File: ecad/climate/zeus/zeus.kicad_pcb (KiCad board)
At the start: 2 copper layers, 80 x 45 mm, 73 parts, among them J1 MCV 1,5/ 2-G-3,5, J10 47053-1000, J11 47053-1000, J2 MCV 1,5/ 2-G-3,5, J3 MCV 1,5/ 2-G-3,5, J4 M20-8760342, J5 47053-1000, J6 47053-1000, J7 215079-8, J8 640454-2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

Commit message: Makes pleiades zeus again
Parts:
- added R20: 47k5, Resistor_SMD:R_0603_1608Metric, F.Cu at (162.3, 139.3)
- added R21: 47k5, Resistor_SMD:R_0603_1608Metric, F.Cu at (169.6, 139.3)
- moved Q1 0.76 mm to (159.8, 139.3)
- moved Q2 0.58 mm to (167.0, 139.3)
- moved D1 0.36 mm to (156.8, 139.3)
- moved D2 0.32 mm to (164.1, 139.3)
- renumbered D2 to D1, D1 to D2
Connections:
- net /HEAT1_PWR renamed /12V Low Side 1/12V_SW-
- net /HEAT2_PWR renamed /12V Low Side 2/12V_SW-
- net /UC/HEAT1 renamed /12V Low Side 1/CMD
- net /UC/HEAT2 renamed /12V Low Side 2/CMD
- U2 pad 1: Net-(U2-Pad1) -> (no net)
- U2 pad 10: Net-(U2-Pad10) -> (no net)
- U2 pad 12: Net-(U2-Pad12) -> (no net)
- U2 pad 13: Net-(U2-Pad13) -> (no net)
- U2 pad 14: Net-(U2-Pad14) -> (no net)
- U2 pad 17: Net-(U2-Pad17) -> (no net)
- U2 pad 18: Net-(U2-Pad18) -> (no net)
- U2 pad 19: Net-(U2-Pad19) -> (no net)
- U2 pad 27: Net-(U2-Pad27) -> (no net)
- U2 pad 28: Net-(U2-Pad28) -> (no net)
- U2 pad 29: Net-(U2-Pad29) -> (no net)
- U2 pad 32: Net-(U2-Pad32) -> (no net)
- U2 pad 33: Net-(U2-Pad33) -> (no net)
- U2 pad 34: Net-(U2-Pad34) -> (no net)
- U2 pad 35: Net-(U2-Pad35) -> (no net)
- U2 pad 36: Net-(U2-Pad36) -> (no net)
- U2 pad 37: Net-(U2-Pad37) -> (no net)
- U2 pad 38: Net-(U2-Pad38) -> (no net)
- U2 pad 39: Net-(U2-Pad39) -> (no net)
- U2 pad 4: Net-(U2-Pad4) -> (no net)
- U2 pad 40: Net-(U2-Pad40) -> (no net)
- U2 pad 41: Net-(U2-Pad41) -> (no net)
- U2 pad 42: Net-(U2-Pad42) -> (no net)
- U2 pad 43: Net-(U2-Pad43) -> (no net)
- U2 pad 44: Net-(U2-Pad44) -> (no net)
- U2 pad 45: Net-(U2-Pad45) -> (no net)
- U2 pad 46: Net-(U2-Pad46) -> (no net)
- U2 pad 47: Net-(U2-Pad47) -> (no net)
- U2 pad 48: Net-(U2-Pad48) -> (no net)
- U2 pad 49: Net-(U2-Pad49) -> (no net)
- U2 pad 50: Net-(U2-Pad50) -> (no net)
- U2 pad 51: Net-(U2-Pad51) -> (no net)
- U2 pad 54: Net-(U2-Pad54) -> (no net)
- U2 pad 55: Net-(U2-Pad55) -> (no net)
- U2 pad 56: Net-(U2-Pad56) -> (no net)
- U2 pad 57: Net-(U2-Pad57) -> (no net)
- U2 pad 58: Net-(U2-Pad58) -> (no net)
- U2 pad 59: Net-(U2-Pad59) -> (no net)
- U2 pad 60: Net-(U2-Pad60) -> (no net)
- U2 pad 61: Net-(U2-Pad61) -> (no net)
- U2 pad 62: Net-(U2-Pad62) -> (no net)
- U2 pad 7: Net-(U2-Pad7) -> (no net)
- U2 pad 9: Net-(U2-Pad9) -> (no net)
- U3 pad 5: Net-(U3-Pad5) -> (no net)
- U5 pad 15: Net-(U5-Pad15) -> (no net)
- U5 pad 16: Net-(U5-Pad16) -> (no net)
- U6 pad 4: /Fan PWM Controller 1/PWM1 -> GND
- U6 pad 5: (no net) -> /Fan PWM Controller 1/PWM1
- U61 pad 4: /Fan PWM Controller 2/PWM1 -> GND
- U61 pad 5: (no net) -> /Fan PWM Controller 2/PWM1
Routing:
- net GND: track 466.1 -> 501.3 mm
- net /12V Low Side 2/CMD: track 27.9 -> 29.3 mm
- net /12V Low Side 1/CMD: track 23.6 -> 24.7 mm
- net /12V Low Side 2/12V_SW-: track 9.40 -> 8.52 mm
- net /12V Low Side 1/12V_SW-: track 9.40 -> 8.70 mm
- net /Fan PWM Controller 2/PWM1: track 15.4 -> 15.9 mm
- net +12V: track 124.4 -> 123.9 mm
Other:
- board text added: "FORT Zeus rev A"
- board text removed: "FORT Pleiades rev A"

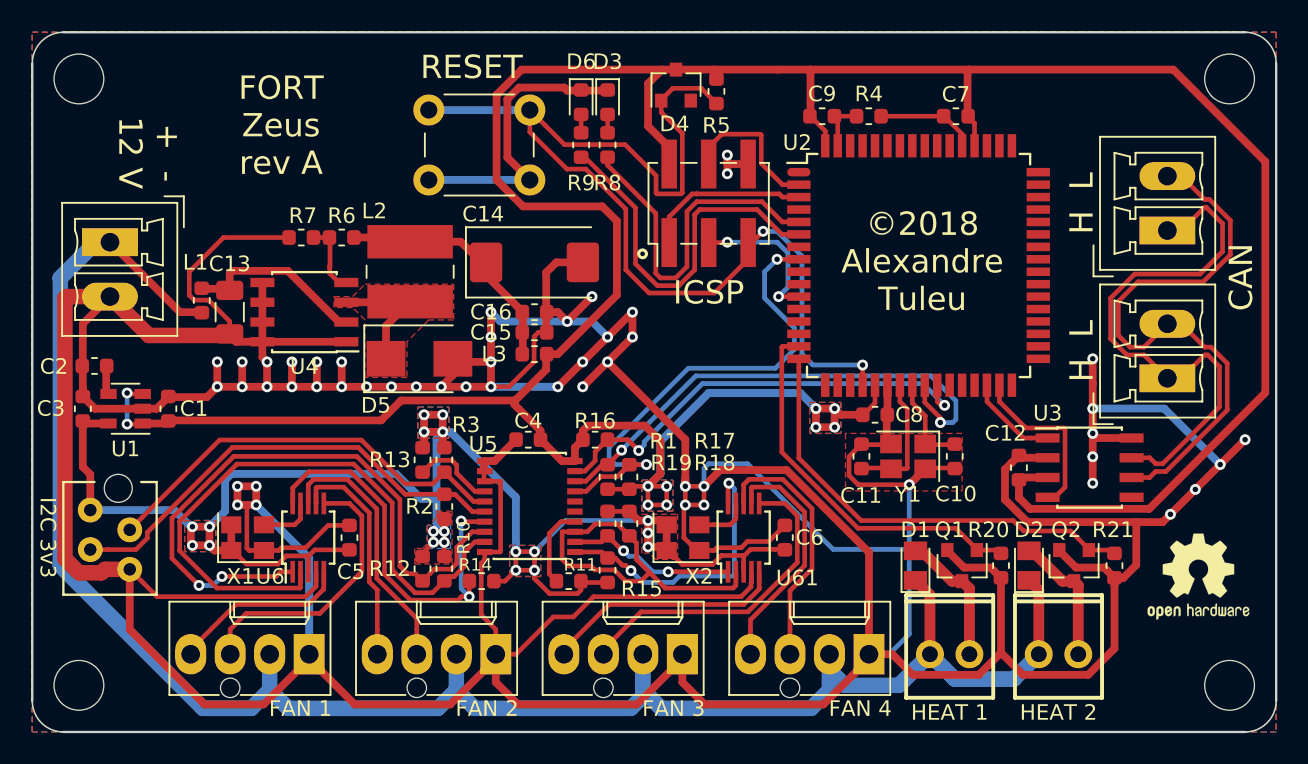
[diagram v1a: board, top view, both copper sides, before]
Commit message: Updates Via size to conform to Factory Capabilities
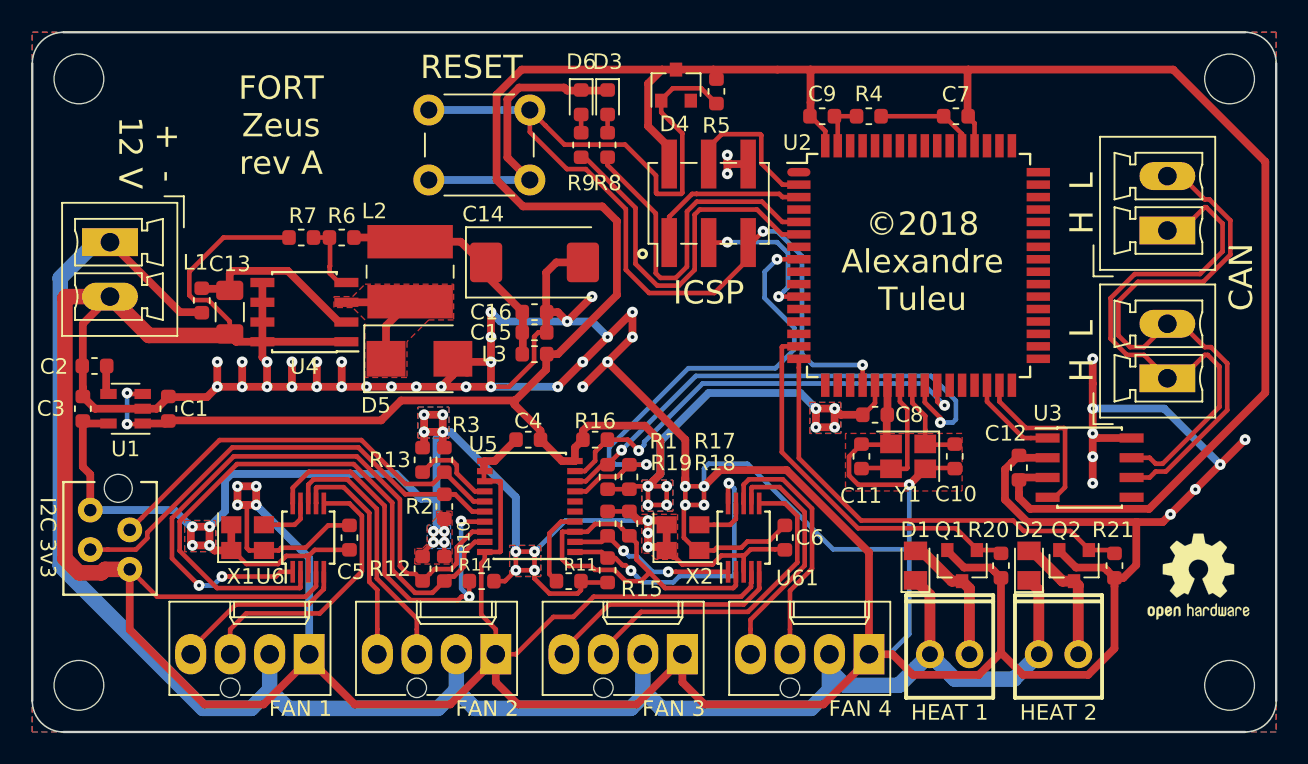
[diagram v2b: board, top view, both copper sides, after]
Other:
- net class Default: via_drill 0.35 -> 0.25
- net class Power: via_drill 0.35 -> 0.25
- rule via_min_drill: 0.35 -> 0.25

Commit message: Small Correction for Production
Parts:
- D1, D2: value MCL4148 -> 1N4148WS; footprint Diode_SMD:D_MicroMELF -> Diode_SMD:D_SOD-323F
- R7: value 4k7 -> 4k87
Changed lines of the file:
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@@
     (visible_elements FFFFFF7F)
     (pcbplotparams
-      (layerselection 0x00030_80000001)
-      (usegerberextensions false)
+      (layerselection 0x010fc_ffffffff)
+      (usegerberextensions true)
       (usegerberattributes false)
       (usegerberadvancedattributes false)
@@
       (psa4output false)
       (plotreference true)
-      (plotvalue true)
+      (plotvalue false)
       (plotinvisibletext false)
       (padsonsilk false)
@@
       (outputformat 1)
       (mirror false)
-      (drillshape 1)
+      (drillshape 0)
       (scaleselection 1)
-      (outputdirectory ""))
+      (outputdirectory "output/"))
   )
   (net 0 "")
@@
     )
   )
-  (module Diode_SMD:D_MicroMELF (layer F.Cu)
-    (at 164.1 139.3 90)
-    (descr "Diode, MicroMELF, http://www.vishay.com/docs/85597/bzm55-se.pdf")
-    (tags "MicroMELF Diode")
-    (attr smd)
-    (fp_text reference D2 (at 2.3 0 180) (layer F.SilkS)
-      (effects (font (size 1 1) (thickness 0.15)))
-    )
-    (fp_text value MCL4148 (at 0 1.8 90) (layer F.Fab)
-      (effects (font (size 1 1) (thickness 0.15)))
-    )
-    (fp_line (start 1.8 1) (end -1.8 1) (layer F.CrtYd) (width 0.05))
-    (fp_line (start 1.8 1) (end 1.8 -1) (layer F.CrtYd) (width 0.05))
-    (fp_line (start -1.8 -1) (end -1.8 1) (layer F.CrtYd) (width 0.05))
-    (fp_line (start -1.8 -1) (end 1.8 -1) (layer F.CrtYd) (width 0.05))
-    (fp_line (start -1.1 0.55) (end -1.1 -0.55) (layer F.Fab) (width 0.12))
-    (fp_line (start 1.1 0.55) (end -1.1 0.55) (layer F.Fab) (width 0.12))
-    (fp_line (start 1.1 -0.55) (end 1.1 0.55) (layer F.Fab) (width 0.12))
-    (fp_line (start -1.1 -0.55) (end 1.1 -0.55) (layer F.Fab) (width 0.12))
-    (fp_line (start -0.6 -0.55) (end -0.6 0.55) (layer F.Fab) (width 0.12))
-    (fp_text user %R (at 0 -1.7 90) (layer F.Fab)
-      (effects (font (size 1 1) (thickness 0.15)))
-    )
-    (fp_line (start -0.25 -0.25) (end -0.25 0.25) (layer F.Fab) (width 0.12))
-    (fp_line (start -0.25 0) (end -0.75 0) (layer F.Fab) (width 0.12))
-    (fp_line (start 0.25 0.25) (end -0.25 0) (layer F.Fab) (width 0.12))
-    (fp_line (start 0.25 -0.25) (end 0.25 0.25) (layer F.Fab) (width 0.12))
-    (fp_line (start -0.25 0) (end 0.25 -0.25) (layer F.Fab) (width 0.12))
-    (fp_line (start 0.25 0) (end 0.75 0) (layer F.Fab) (width 0.12))
-    (fp_line (start -1.7 0.9) (end 1.1 0.9) (layer F.SilkS) (width 0.12))
-    (fp_line (start -1.7 -0.9) (end -1.7 0.9) (layer F.SilkS) (width 0.12))
-    (fp_line (start 1.1 -0.9) (end -1.7 -0.9) (layer F.SilkS) (width 0.12))
-    (pad 2 smd rect (at 0.95 0 90) (size 1.2 1.5) (layers F.Cu F.Paste F.Mask)
-      (net 49 "/12V Low Side 2/12V_SW-"))
-    (pad 1 smd rect (at -0.95 0 90) (size 1.2 1.5) (layers F.Cu F.Paste F.Mask)
-      (net 8 +12V))
-    (model ${KISYS3DMOD}/Diode_SMD.3dshapes/D_MicroMELF.wrl
-      (at (xyz 0 0 0))
-      (scale (xyz 1 1 1))
-      (rotate (xyz 0 0 0))
-    )
-  )
-  (module Diode_SMD:D_MicroMELF (layer F.Cu)
-    (at 156.8 139.3 90)
-    (descr "Diode, MicroMELF, http://www.vishay.com/docs/85597/bzm55-se.pdf")
-    (tags "MicroMELF Diode")
-    (attr smd)
-    (fp_text reference D1 (at 2.3 0 180) (layer F.SilkS)
-      (effects (font (size 1 1) (thickness 0.15)))
-    )
-    (fp_text value MCL4148 (at 0 1.8 90) (layer F.Fab)
-      (effects (font (size 1 1) (thickness 0.15)))
-    )
-    (fp_line (start 1.8 1) (end -1.8 1) (layer F.CrtYd) (width 0.05))
-    (fp_line (start 1.8 1) (end 1.8 -1) (layer F.CrtYd) (width 0.05))
-    (fp_line (start -1.8 -1) (end -1.8 1) (layer F.CrtYd) (width 0.05))
-    (fp_line (start -1.8 -1) (end 1.8 -1) (layer F.CrtYd) (width 0.05))
-    (fp_line (start -1.1 0.55) (end -1.1 -0.55) (layer F.Fab) (width 0.12))
-    (fp_line (start 1.1 0.55) (end -1.1 0.55) (layer F.Fab) (width 0.12))
-    (fp_line (start 1.1 -0.55) (end 1.1 0.55) (layer F.Fab) (width 0.12))
-    (fp_line (start -1.1 -0.55) (end 1.1 -0.55) (layer F.Fab) (width 0.12))
-    (fp_line (start -0.6 -0.55) (end -0.6 0.55) (layer F.Fab) (width 0.12))
-    (fp_text user %R (at 0 -1.7 90) (layer F.Fab)
-      (effects (font (size 1 1) (thickness 0.15)))
-    )
-    (fp_line (start -0.25 -0.25) (end -0.25 0.25) (layer F.Fab) (width 0.12))
-    (fp_line (start -0.25 0) (end -0.75 0) (layer F.Fab) (width 0.12))
-    (fp_line (start 0.25 0.25) (end -0.25 0) (layer F.Fab) (width 0.12))
-    (fp_line (start 0.25 -0.25) (end 0.25 0.25) (layer F.Fab) (width 0.12))
-    (fp_line (start -0.25 0) (end 0.25 -0.25) (layer F.Fab) (width 0.12))
-    (fp_line (start 0.25 0) (end 0.75 0) (layer F.Fab) (width 0.12))
-    (fp_line (start -1.7 0.9) (end 1.1 0.9) (layer F.SilkS) (width 0.12))
-    (fp_line (start -1.7 -0.9) (end -1.7 0.9) (layer F.SilkS) (width 0.12))
-    (fp_line (start 1.1 -0.9) (end -1.7 -0.9) (layer F.SilkS) (width 0.12))
-    (pad 2 smd rect (at 0.95 0 90) (size 1.2 1.5) (layers F.Cu F.Paste F.Mask)
-      (net 48 "/12V Low Side 1/12V_SW-"))
-    (pad 1 smd rect (at -0.95 0 90) (size 1.2 1.5) (layers F.Cu F.Paste F.Mask)
-      (net 8 +12V))
-    (model ${KISYS3DMOD}/Diode_SMD.3dshapes/D_MicroMELF.wrl
-      (at (xyz 0 0 0))
-      (scale (xyz 1 1 1))
-      (rotate (xyz 0 0 0))
-    )
-  )
   (module LED_SMD:LED_0603_1608Metric (layer F.Cu)
     (at 137 109.5 270)
@@
       (effects (font (size 1 1) (thickness 0.15)))
     )
-    (fp_text value 4k7 (at 0 1.43 180) (layer F.Fab)
+    (fp_text value 4k87 (at 0 1.43 180) (layer F.Fab)
       (effects (font (size 1 1) (thickness 0.15)))
     )
@@
       (at (xyz 0 0 0))
       (scale (xyz 1 1 1))
+      (rotate (xyz 0 0 0))
+    )
+  )
+  (module Diode_SMD:D_SOD-323F (layer F.Cu)
+    (at 156.8 139.3 90)
+    (descr "SOD-323F http://www.nxp.com/documents/outline_drawing/SOD323F.pdf")
+    (tags SOD-323F)
+    (attr smd)
+    (fp_text reference D1 (at 2.3 -0.05 180) (layer F.SilkS)
+      (effects (font (size 1 1) (thickness 0.15)))
+    )
+    (fp_text value 1N4148WS (at 0.1 1.9 90) (layer F.Fab)
+      (effects (font (size 1 1) (thickness 0.15)))
+    )
+    (fp_line (start -1.5 -0.85) (end 1.05 -0.85) (layer F.SilkS) (width 0.12))
+    (fp_line (start -1.5 0.85) (end 1.05 0.85) (layer F.SilkS) (width 0.12))
+    (fp_line (start -1.6 -0.95) (end -1.6 0.95) (layer F.CrtYd) (width 0.05))
+    (fp_line (start -1.6 0.95) (end 1.6 0.95) (layer F.CrtYd) (width 0.05))
+    (fp_line (start 1.6 -0.95) (end 1.6 0.95) (layer F.CrtYd) (width 0.05))
+    (fp_line (start -1.6 -0.95) (end 1.6 -0.95) (layer F.CrtYd) (width 0.05))
+    (fp_line (start -0.9 -0.7) (end 0.9 -0.7) (layer F.Fab) (width 0.1))
+    (fp_line (start 0.9 -0.7) (end 0.9 0.7) (layer F.Fab) (width 0.1))
+    (fp_line (start 0.9 0.7) (end -0.9 0.7) (layer F.Fab) (width 0.1))
+    (fp_line (start -0.9 0.7) (end -0.9 -0.7) (layer F.Fab) (width 0.1))
+    (fp_line (start -0.3 -0.35) (end -0.3 0.35) (layer F.Fab) (width 0.1))
+    (fp_line (start -0.3 0) (end -0.5 0) (layer F.Fab) (width 0.1))
+    (fp_line (start -0.3 0) (end 0.2 -0.35) (layer F.Fab) (width 0.1))
+    (fp_line (start 0.2 -0.35) (end 0.2 0.35) (layer F.Fab) (width 0.1))
+    (fp_line (start 0.2 0.35) (end -0.3 0) (layer F.Fab) (width 0.1))
+    (fp_line (start 0.2 0) (end 0.45 0) (layer F.Fab) (width 0.1))
+    (fp_line (start -1.5 -0.85) (end -1.5 0.85) (layer F.SilkS) (width 0.12))
+    (fp_text user %R (at 0 -1.85 90) (layer F.Fab)
+      (effects (font (size 1 1) (thickness 0.15)))
+    )
+    (pad 2 smd rect (at 1.1 0 90) (size 0.5 0.5) (layers F.Cu F.Paste F.Mask)
+      (net 48 "/12V Low Side 1/12V_SW-"))
+    (pad 1 smd rect (at -1.1 0 90) (size 0.5 0.5) (layers F.Cu F.Paste F.Mask)
+      (net 8 +12V))
+    (model ${KISYS3DMOD}/Diode_SMD.3dshapes/D_SOD-323F.wrl
+      (at (xyz 0 0 0))
+      (scale (xyz 1 1 1))
+      (rotate (xyz 0 0 0))
+    )
+  )
+  (module Diode_SMD:D_SOD-323F (layer F.Cu)
+    (at 164.1 139.3 90)
+    (descr "SOD-323F http://www.nxp.com/documents/outline_drawing/SOD323F.pdf")
+    (tags SOD-323F)
+    (attr smd)
+    (fp_text reference D2 (at 2.3 0 180) (layer F.SilkS)
+      (effects (font (size 1 1) (thickness 0.15)))
+    )
+    (fp_text value 1N4148WS (at 0.1 1.9 90) (layer F.Fab)
+      (effects (font (size 1 1) (thickness 0.15)))
+    )
+    (fp_text user %R (at 0 -1.85 90) (layer F.Fab)
+      (effects (font (size 1 1) (thickness 0.15)))
+    )
+    (fp_line (start -1.5 -0.85) (end -1.5 0.85) (layer F.SilkS) (width 0.12))
+    (fp_line (start 0.2 0) (end 0.45 0) (layer F.Fab) (width 0.1))
+    (fp_line (start 0.2 0.35) (end -0.3 0) (layer F.Fab) (width 0.1))
+    (fp_line (start 0.2 -0.35) (end 0.2 0.35) (layer F.Fab) (width 0.1))
+    (fp_line (start -0.3 0) (end 0.2 -0.35) (layer F.Fab) (width 0.1))
+    (fp_line (start -0.3 0) (end -0.5 0) (layer F.Fab) (width 0.1))
+    (fp_line (start -0.3 -0.35) (end -0.3 0.35) (layer F.Fab) (width 0.1))
+    (fp_line (start -0.9 0.7) (end -0.9 -0.7) (layer F.Fab) (width 0.1))
+    (fp_line (start 0.9 0.7) (end -0.9 0.7) (layer F.Fab) (width 0.1))
+    (fp_line (start 0.9 -0.7) (end 0.9 0.7) (layer F.Fab) (width 0.1))
+    (fp_line (start -0.9 -0.7) (end 0.9 -0.7) (layer F.Fab) (width 0.1))
+    (fp_line (start -1.6 -0.95) (end 1.6 -0.95) (layer F.CrtYd) (width 0.05))
+    (fp_line (start 1.6 -0.95) (end 1.6 0.95) (layer F.CrtYd) (width 0.05))
+    (fp_line (start -1.6 0.95) (end 1.6 0.95) (layer F.CrtYd) (width 0.05))
+    (fp_line (start -1.6 -0.95) (end -1.6 0.95) (layer F.CrtYd) (width 0.05))
+    (fp_line (start -1.5 0.85) (end 1.05 0.85) (layer F.SilkS) (width 0.12))
+    (fp_line (start -1.5 -0.85) (end 1.05 -0.85) (layer F.SilkS) (width 0.12))
+    (pad 1 smd rect (at -1.1 0 90) (size 0.5 0.5) (layers F.Cu F.Paste F.Mask)
+      (net 8 +12V))
+    (pad 2 smd rect (at 1.1 0 90) (size 0.5 0.5) (layers F.Cu F.Paste F.Mask)
+      (net 49 "/12V Low Side 2/12V_SW-"))
+    (model ${KISYS3DMOD}/Diode_SMD.3dshapes/D_SOD-323F.wrl
+      (at (xyz 0 0 0))
+      (scale (xyz 1 1 1))

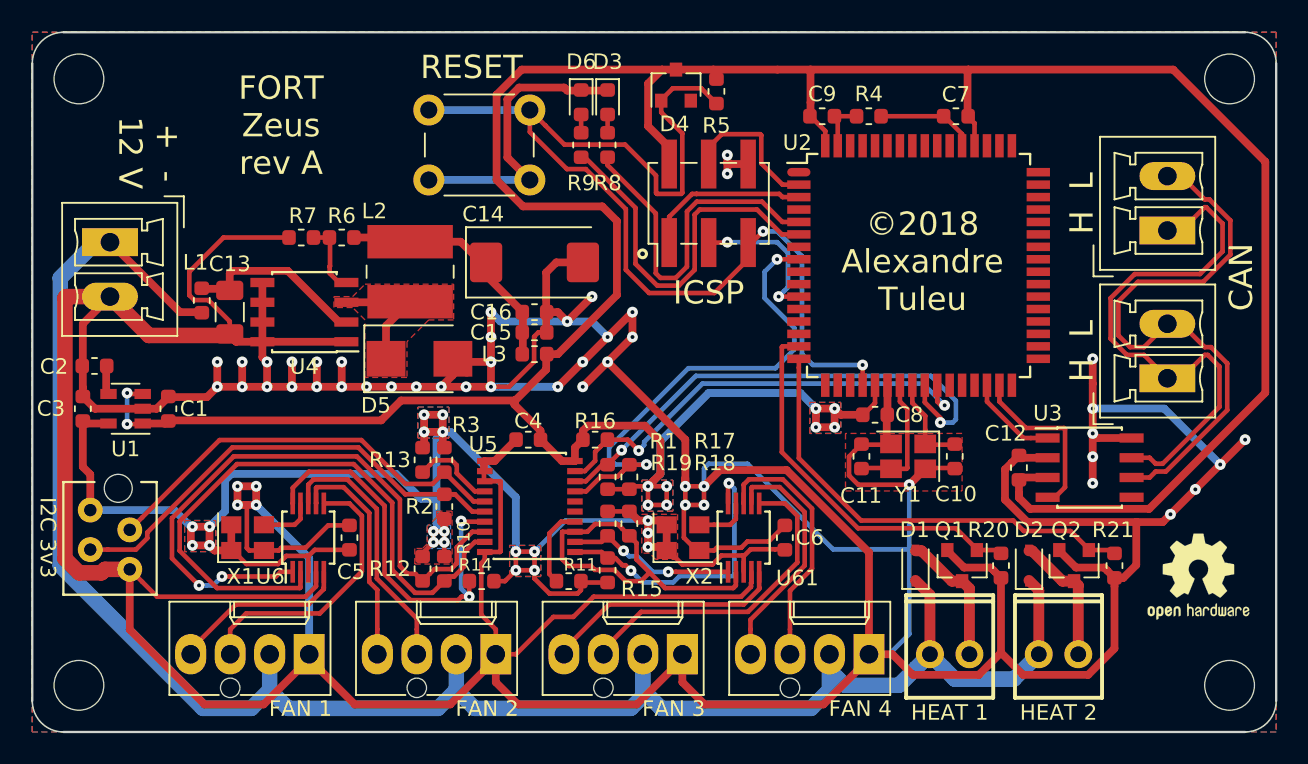
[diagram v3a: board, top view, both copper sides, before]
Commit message: Changes via fpr ,ultiple factory capabilities
To be both eurocircuit and pcbway low price compatible, via should be
0.75/0.3 mm sized.
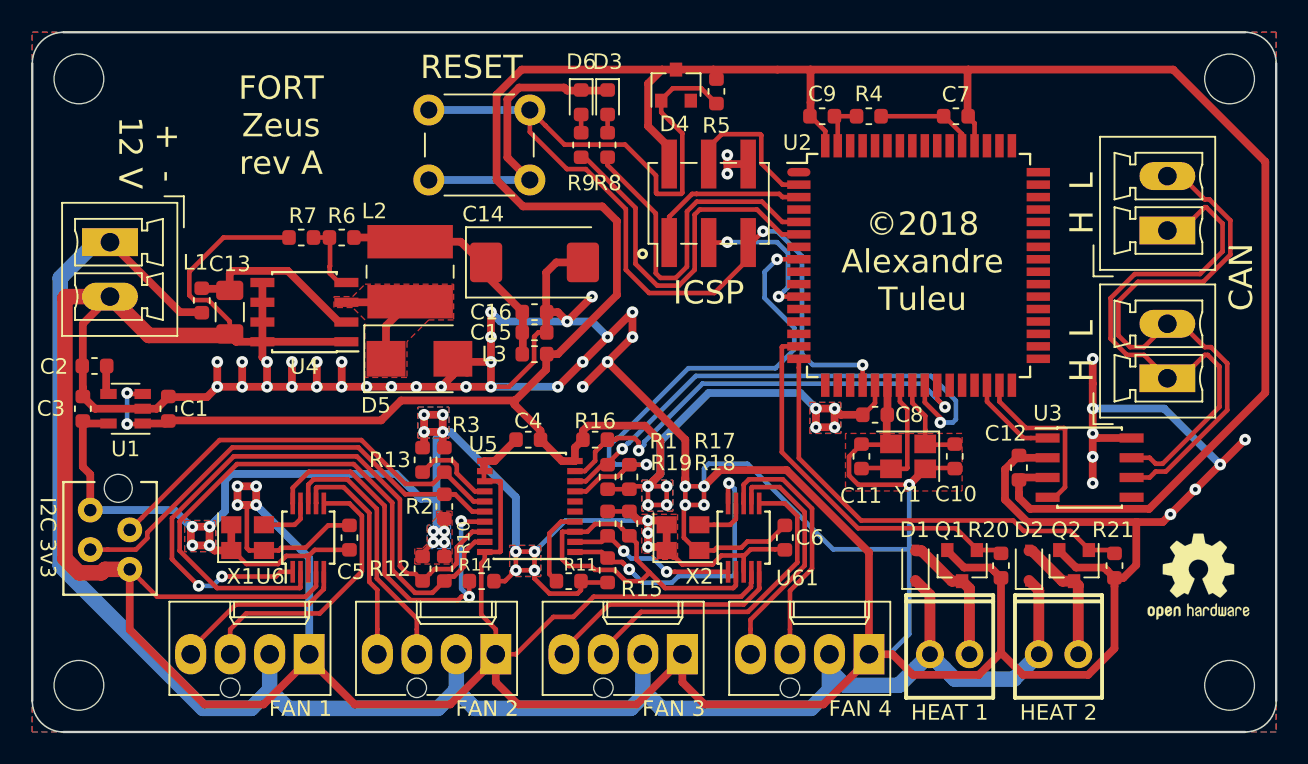
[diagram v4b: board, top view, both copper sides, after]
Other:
- net class Default: via_dia 0.7 -> 0.75; via_drill 0.25 -> 0.3
- net class Power: via_dia 0.7 -> 0.75; via_drill 0.25 -> 0.3

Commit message: Licenses Climate PCB under OHL v1.2
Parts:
- added G***: LOGO, FORT:UNIL-LOGO_9.2x3, F.Cu at (175.0, 143.2)
- moved REF*** 2.15 mm to (176.2, 138.2)
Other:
- board text added: "©2018 Université de Lausanne"
- board text removed: "©2018 Alexandre Tuleu"
